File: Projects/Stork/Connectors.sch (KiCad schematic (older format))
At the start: 24 parts, among them J1 Conn_01x05, J10 Conn_01x05, J11 Conn_01x05, J12 Conn_01x05, J13 Conn_01x05, J14 Conn_01x05, J15 Conn_01x05, J16 Conn_01x05, J17 Conn_01x05, J18 Conn_01x05, J19 Conn_01x05, J2 Conn_01x05, J20 Conn_01x05, J21 Conn_01x05, J22 Conn_01x05, J23 Conn_01x05, J24 Conn_01x05, J3 Conn_01x05, J4 Conn_01x05, J5 Conn_01x05, J6 Conn_01x05, J7 Conn_01x05, J8 Conn_01x05, J9 Conn_01x05

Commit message: changed position of cora z7 to be at center with cutout to give headroom for ethernet and powerjack
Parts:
- removed J1, J10, J11, J12, J13, J14, J15, J16, J17, J18, J19, J2, J20, J21, J22, J23, J24, J3, J4, J5, J6, J7, J8, J9: Conn_01x05, Connector_PinHeader_2.54mm:PinHeader_1x05_P2.54mm_Vertical, symbol Connector_Generic:Conn_01x05
- added J31, J32, J33, J34, J35, J36, J37, J38, J39, J40, J41, J42: Conn_02x05_Top_Bottom, Connector_PinHeader_2.54mm:PinHeader_2x05_P2.54mm_Vertical, symbol Connector_Generic:Conn_02x05_Top_Bottom
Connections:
- net labels removed: GND
- wire segments 144 -> 96

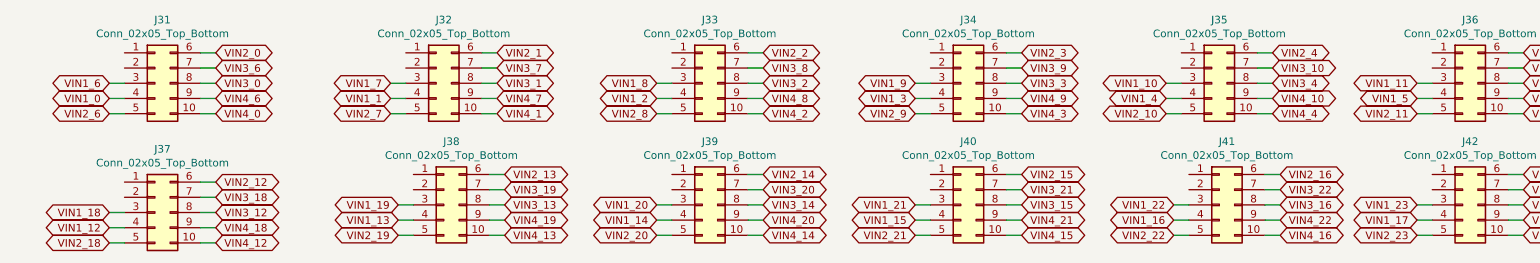
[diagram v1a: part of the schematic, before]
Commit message: Pin headers have pins connected to ground
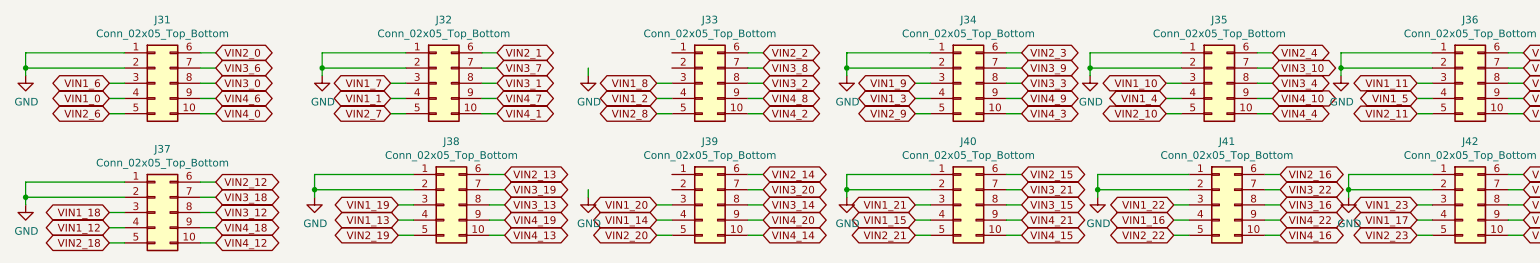
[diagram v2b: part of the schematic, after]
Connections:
- net GND: now reaches J31.1 (Pin_1)
- net GND: now also J31.2 (Pin_2), J32.1 (Pin_1), J32.2 (Pin_2), J34.1 (Pin_1), J34.2 (Pin_2), J35.1 (Pin_1), J35.2 (Pin_2), J36.1 (Pin_1), J36.2 (Pin_2), J37.1 (Pin_1), J37.2 (Pin_2), J38.1 (Pin_1), J38.2 (Pin_2), J40.1 (Pin_1), J40.2 (Pin_2), J41.1 (Pin_1), J41.2 (Pin_2), J42.1 (Pin_1), J42.2 (Pin_2)
